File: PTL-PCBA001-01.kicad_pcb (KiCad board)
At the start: 2 copper layers, 67.5 x 120 mm, 39 parts, among them J1 SJ-43514-SMT, J2 CONN_01X03, J3 CONN_01X02, SW1 SW_Push_LED, SW2 1-1825027-1, U1 74AUC1G66, U2 74AUC1G66, U3 PARTICLE_PHOTON, U4 NRF24L01+_MOD, U5 A1324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

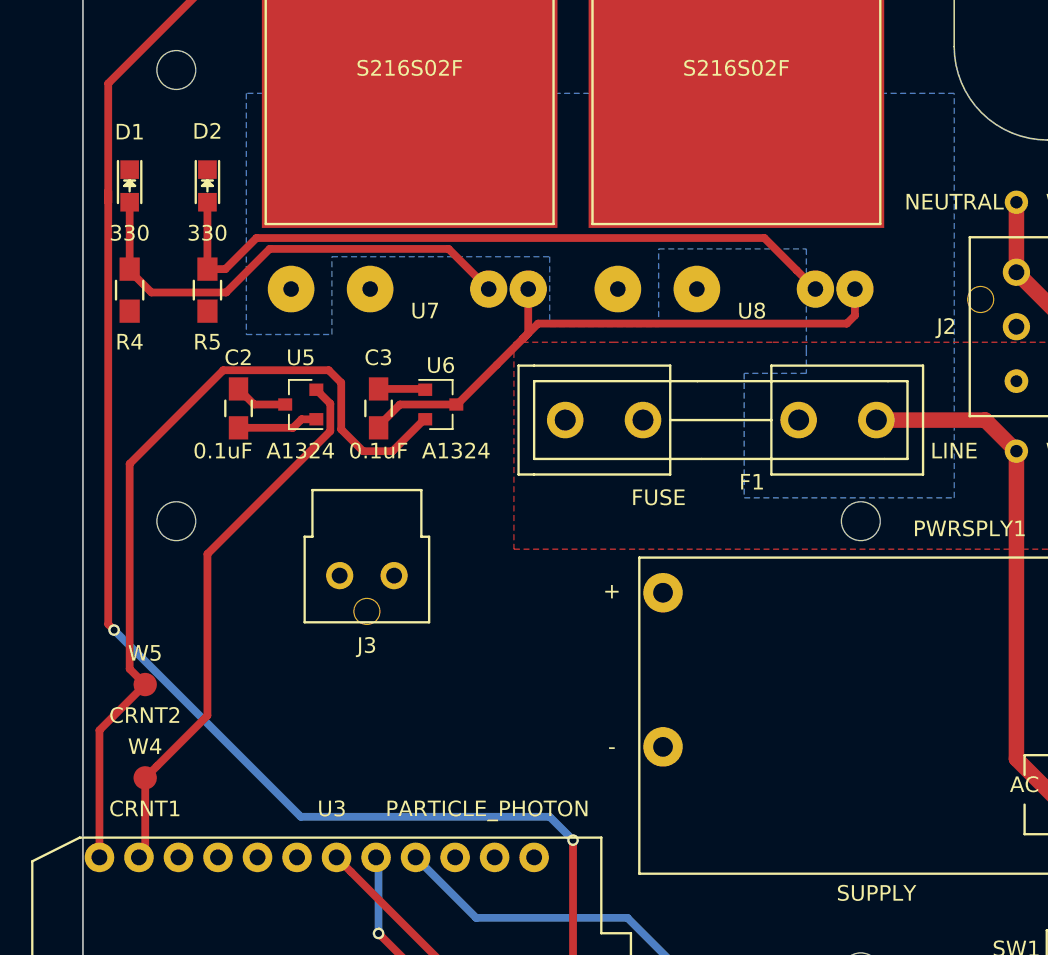
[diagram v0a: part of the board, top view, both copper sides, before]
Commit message: Added ground pours for PWR 1 and PWR 2
Rearranged a current sensor output and SSR control pins for cleaner
routing
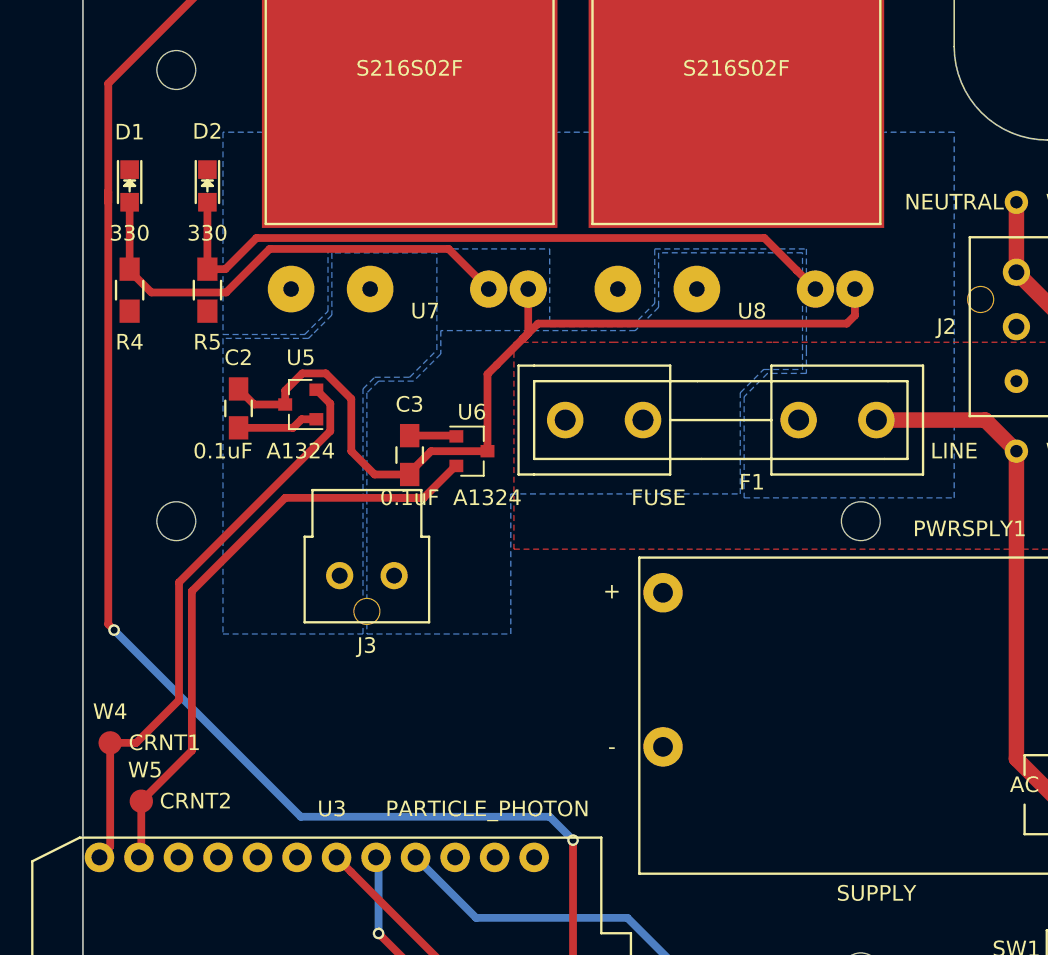
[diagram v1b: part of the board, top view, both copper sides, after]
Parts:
- moved W5 7.50 mm to (123.8, 92.5)
- moved C3 3.61 mm to (141.0, 70.2)
- moved U6 3.61 mm to (145.0, 70.0)
- moved W4 3.18 mm to (121.8, 88.8)
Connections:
- R4 pad 1: /PIN20 -> /PIN19
- R5 pad 1: /PIN19 -> /PIN20
- U3 pad 11: /CRNT1 -> /CRNT2
- U3 pad 12: /CRNT2 -> /CRNT1
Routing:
- net GND: track 46.3 -> 62.5 mm
- net /CRNT2: track 53.2 -> 41.0 mm
- net /CRNT1: track 35.5 -> 37.6 mm
- added copper zone on B.Cu, net /PWR1
- added copper zone on B.Cu, net /PWR2

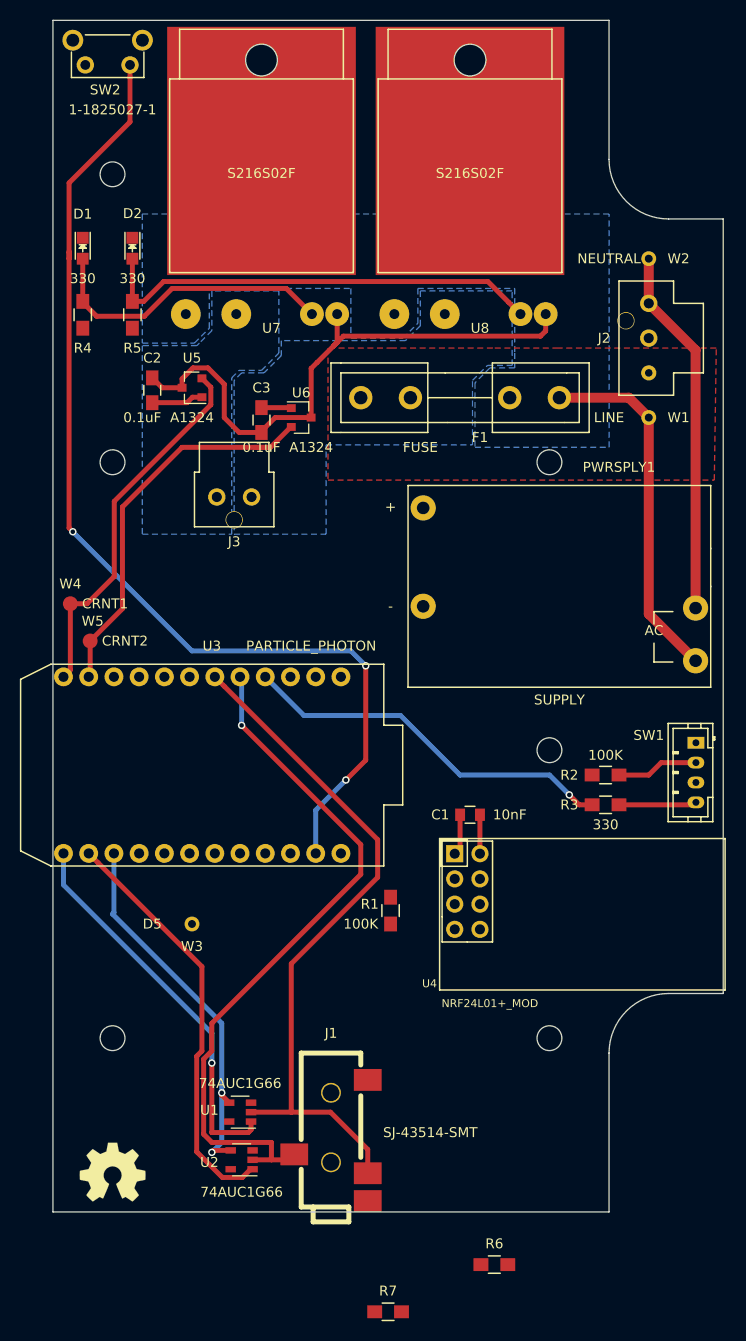
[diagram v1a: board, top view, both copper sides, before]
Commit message: Routed OMNI_SW, broke reset trace
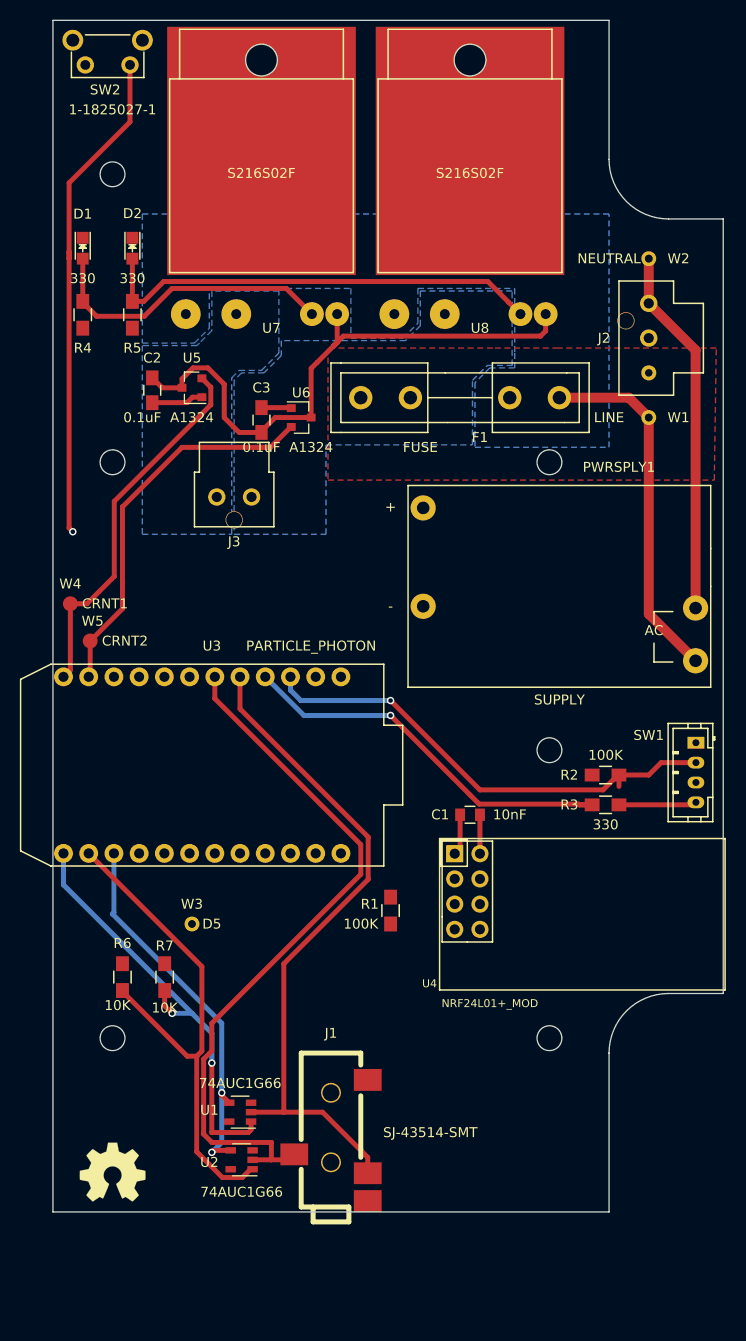
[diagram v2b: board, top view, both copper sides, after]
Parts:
- moved R6 47.3 mm to (127.0, 126.3), turned to 270 degrees
- moved R7 40.5 mm to (131.2, 126.3), turned to 270 degrees
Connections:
- J1 pad 3: /PIN5 -> /PIN6
- J1 pad 4: /PIN6 -> /PIN5
- U1 pad 2: /PIN6 -> /PIN5
- U2 pad 2: /PIN5 -> /PIN6
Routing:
- net /PIN23: track 106.5 -> 50.4 mm, vias 3 -> 1
- net /OMNI_SW: track 8.27 -> 48.6 mm, vias 0 -> 1
- net /PIN14: track 42.0 -> 52.3 mm
- net /PIN13: track 39.2 -> 43.8 mm, vias 1 -> 2
- net /PIN5: track 71.0 -> 68.2 mm, vias 1 -> 0
- net /PIN6: track 69.9 -> 72.0 mm
- net /OMNI_LED: track 38.3 -> 39.5 mm

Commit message: Added ground pour
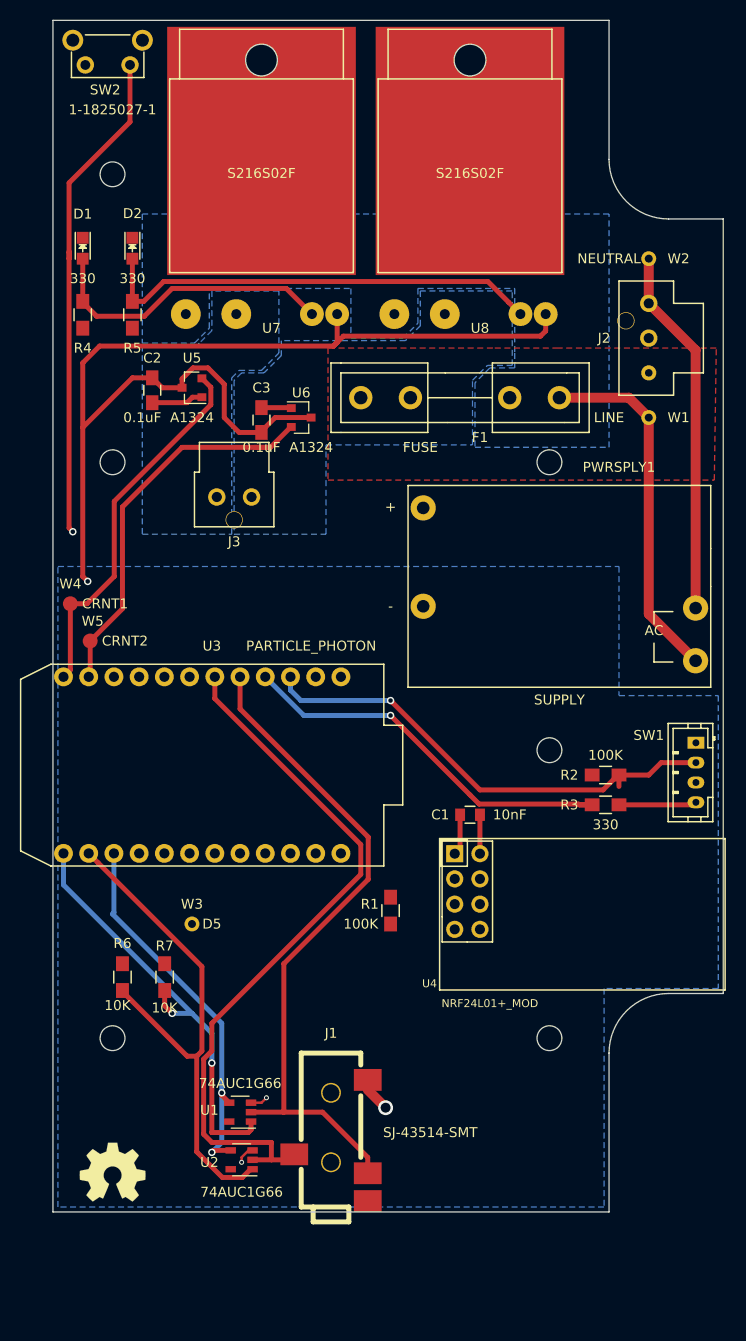
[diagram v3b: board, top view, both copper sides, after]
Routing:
- net GND: track 62.5 -> 118.8 mm, vias 0 -> 4
- added copper zone on B.Cu, net GND
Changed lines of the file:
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@@
   (general
     (links 76)
-    (no_connects 34)
+    (no_connects 26)
     (area 119.949999 29.949999 187.550001 150.050001)
     (thickness 1.6)
     (drawings 11)
-    (tracks 163)
+    (tracks 178)
     (zones 0)
     (modules 39)
@@
   )
   (setup
-    (last_trace_width 0.25)
+    (last_trace_width 0.5)
     (user_trace_width 0.25)
     (user_trace_width 0.5)
@@
   (gr_arc (start 182 44) (end 176 44) (angle -90) (layer Edge.Cuts) (width 0.1))
   (gr_line (start 120 30) (end 176 30) (layer Edge.Cuts) (width 0.1))
-  (segment (start 146 70) (end 146 65.05) (width 0.5) (layer F.Cu) (net 1))
-  (segment (start 146 65.05) (end 146.6 64.45) (width 0.5) (layer F.Cu) (net 1))
+  (segment (start 123 64.5) (end 123 71) (width 0.5) (layer F.Cu) (net 1))
+  (segment (start 123 71) (end 123 86) (width 0.5) (layer F.Cu) (net 1))
+  (segment (start 130 66) (end 128 66) (width 0.5) (layer F.Cu) (net 1))
+  (segment (start 128 66) (end 123 71) (width 0.5) (layer F.Cu) (net 1))
+  (segment (start 148.25 62.8) (end 124.7 62.8) (width 0.5) (layer F.Cu) (net 1))
+  (segment (start 124.7 62.8) (end 123 64.5) (width 0.5) (layer F.Cu) (net 1))
+  (segment (start 123 86) (end 123.5 86.5) (width 0.5) (layer F.Cu) (net 1))
+  (via (at 123.5 86.5) (size 0.75) (drill 0.45) (layers F.Cu B.Cu) (net 1))
+  (segment (start 151.7 136.7) (end 151.7 137.7) (width 0.5) (layer F.Cu) (net 1) (status C00000))
+  (segment (start 151.7 137.7) (end 153.5 139.5) (width 1) (layer F.Cu) (net 1) (status 400000))
+  (via (at 153.5 139.5) (size 1.5) (drill 1) (layers F.Cu B.Cu) (net 1))
+  (segment (start 140.1 143.8) (end 139.7 143.8) (width 0.25) (layer F.Cu) (net 1) (status C00000))
+  (segment (start 139.7 143.8) (end 139 144.5) (width 0.25) (layer F.Cu) (net 1) (status 400000))
+  (segment (start 139 144.5) (end 139 145) (width 0.25) (layer F.Cu) (net 1))
+  (via (at 139 145) (size 0.5) (drill 0.3) (layers F.Cu B.Cu) (net 1))
+  (segment (start 139.95 139) (end 141 139) (width 0.25) (layer F.Cu) (net 1) (status 400000))
+  (segment (start 141 139) (end 141.5 138.5) (width 0.25) (layer F.Cu) (net 1))
+  (via (at 141.5 138.5) (size 0.5) (drill 0.3) (layers F.Cu B.Cu) (net 1))
   (segment (start 137.25 70) (end 138.75 71.5) (width 0.5) (layer F.Cu) (net 1))
   (segment (start 138.75 71.5) (end 141 71.5) (width 0.5) (layer F.Cu) (net 1))
@@
   (segment (start 133 66.1) (end 134.1 65) (width 0.5) (layer F.Cu) (net 1))
   (segment (start 148.62 62.43) (end 148.25 62.8) (width 0.5) (layer F.Cu) (net 1))
-  (segment (start 148.25 62.8) (end 146.6 64.45) (width 0.5) (layer F.Cu) (net 1))
   (segment (start 169.097056 61.8) (end 149.25 61.8) (width 0.5) (layer F.Cu) (net 1))
   (segment (start 149.25 61.8) (end 148.25 62.8) (width 0.5) (layer F.Cu) (net 1))
@@
       )
     )
+  )
+  (zone (net 1) (net_name GND) (layer B.Cu) (hatch edge 0.508)
+    (connect_pads (clearance 0.508))
+    (min_thickness 0.254)
+    (fill yes (arc_segments 16) (thermal_gap 0.508) (thermal_bridge_width 0.5))
+    (polygon
+      (pts
+        (xy 177 98) (xy 187 98) (xy 187 127.5) (xy 175.5 127.5) (xy 175.5 149.5)
+        (xy 120.5 149.5) (xy 120.5 85) (xy 177 85)
+      )
+    )

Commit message: Finish rev A design, created gerbers
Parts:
- added R10: 10K, Resistors_SMD:R_0805_HandSoldering, F.Cu at (163.0, 133.6)
- added R11: 10K, Resistors_SMD:R_0805_HandSoldering, F.Cu at (155.5, 133.6)
- added R12: 10K, Resistors_SMD:R_0805_HandSoldering, F.Cu at (165.8, 133.6)
- added R8: 10K, Resistors_SMD:R_0805_HandSoldering, F.Cu at (160.5, 133.6)
- added R9: 10K, Resistors_SMD:R_0805_HandSoldering, F.Cu at (158.0, 133.6)
- moved R1 11.5 mm to (142.5, 119.3), turned to 270 degrees
- moved W4 1.77 mm to (122.0, 90.5)
- moved C3 1.00 mm to (140.0, 70.2)
- moved U6 1.00 mm to (144.0, 70.0)
- moved U5 0.71 mm to (134.5, 67.5), turned to 0 degrees
- turned C2 to 270 degrees
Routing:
- net /PIN20: track 0.00 -> 97.9 mm, vias 0 -> 4
- net /PIN19: track 0.00 -> 96.6 mm, vias 0 -> 4
- net +3V3: track 12.3 -> 90.4 mm, vias 0 -> 6
- net /PIN23: track 50.4 -> 127.4 mm, vias 1 -> 4
- net /NRF_SS: track 0.00 -> 64.6 mm, vias 0 -> 1
- net /PIN9: track 0.00 -> 61.4 mm, vias 0 -> 2
- net /MOSI: track 0.00 -> 56.8 mm
- net /MISO: track 0.00 -> 56.5 mm, vias 0 -> 1
- net /NRF_IRQ: track 0.00 -> 46.3 mm, vias 0 -> 2
- net /NRF_EN: track 0.00 -> 37.8 mm, vias 0 -> 3
- net GND: track 118.8 -> 148.0 mm, vias 4 -> 6
- net /CRNT1: track 37.6 -> 32.8 mm
- net /CRNT2: track 41.0 -> 38.4 mm
- net /OMNI_SW: track 48.6 -> 47.5 mm
- net /PIN6: track 72.0 -> 72.5 mm, vias 0 -> 1
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- added copper zone on F.Cu, net +3V3
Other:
- board text added: "67.5x120mm"
- board text added: "PTL-PCBA001-01 01/03/2017"
